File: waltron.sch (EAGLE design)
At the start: 26 parts, among them IC1 4049N, IC2 LM386, J1 On Switch, J2 9v battery, J7 8ohm speaker

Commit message: Rip up and lay out board
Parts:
- VR1: device adafruit:TRIM -> SparkFun-Retired:POTTRIM
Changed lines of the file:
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@@
 <setting verticaltext="up"/>
 </settings>
-<grid distance="0.05" unitdist="inch" unit="inch" style="lines" multiple="1" display="no" altdistance="0.01" altunitdist="inch" altunit="inch"/>
+<grid distance="0.1" unitdist="inch" unit="inch" style="lines" multiple="1" display="no" altdistance="0.01" altunitdist="inch" altunit="inch"/>
 <layers>
 <layer number="1" name="Top" color="4" fill="1" visible="no" active="no"/>
@@
 <part name="P+1" library="supply1" deviceset="V+" device=""/>
 <part name="GND1" library="supply1" deviceset="GND" device=""/>
-<part name="VR1" library="adafruit" deviceset="TRIM" device="" value="5K"/>
+<part name="VR1" library="SparkFun-Retired" deviceset="POT" device="TRIM" value="5K"/>
 <part name="J3" library="SparkFun-Connectors" deviceset="CONN_02" device=""/>
 <part name="J4" library="SparkFun-Connectors" deviceset="CONN_02" device=""/>

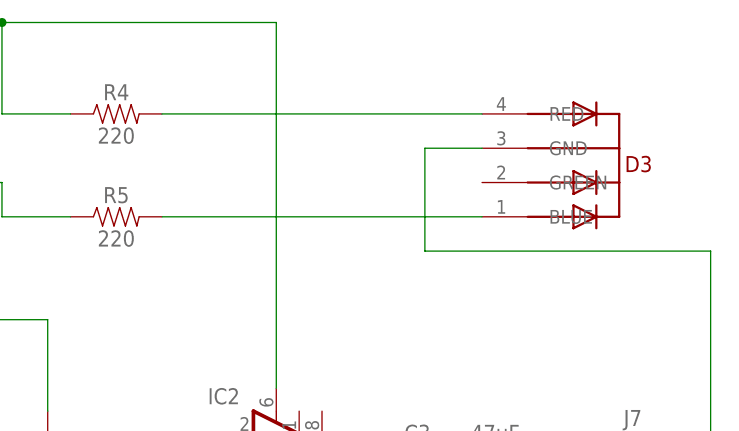
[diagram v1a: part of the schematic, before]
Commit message: Add mounting holes and swap out LED for mirrored version
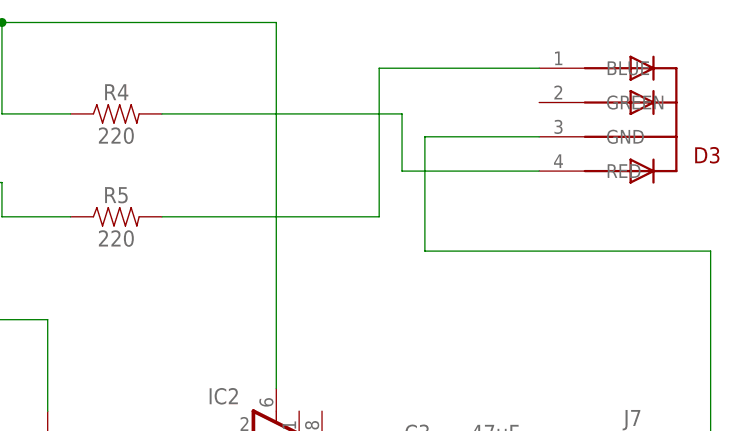
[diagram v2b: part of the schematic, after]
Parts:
- D3: device adafruit:5MMRGBLED -> tommy:5MMRGBLED
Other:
- moved on the sheet: D3
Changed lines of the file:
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@@
 <part name="J5" library="SparkFun-Connectors" deviceset="CONN_02" device=""/>
 <part name="J6" library="SparkFun-Connectors" deviceset="CONN_02" device=""/>
-<part name="D3" library="adafruit" deviceset="5MMRGBLED" device=""/>
+<part name="D3" library="tommy" deviceset="5MMRGBLED" device=""/>
 <part name="J1" library="SparkFun-Connectors" deviceset="CONN_02" device="" value="On Switch"/>
 </parts>
@@
 <attribute name="NAME" x="99.568" y="-5.08" size="1.778" layer="95" font="vector" rot="MR0"/>
 </instance>
-<instance part="D3" gate="G$1" x="208.28" y="72.39" smashed="yes" rot="MR90">
-<attribute name="NAME" x="211.973553125" y="69.741753125" size="1.778" layer="94" rot="MR0"/>
+<instance part="D3" gate="G$1" x="214.63" y="73.66" smashed="yes" rot="R270">
+<attribute name="NAME" x="219.593553125" y="72.498246875" size="1.778" layer="94" rot="R180"/>
 </instance>
 <instance part="J1" gate="G$1" x="-55.88" y="55.88" smashed="yes" rot="MR180">
@@
 <segment>
 <pinref part="R5" gate="G$1" pin="2"/>
-<wire x1="157.48" y1="64.77" x2="193.04" y2="64.77" width="0.1524" layer="91"/>
+<wire x1="157.48" y1="64.77" x2="181.61" y2="64.77" width="0.1524" layer="91"/>
+<wire x1="181.61" y1="64.77" x2="181.61" y2="81.28" width="0.1524" layer="91"/>
+<wire x1="181.61" y1="81.28" x2="199.39" y2="81.28" width="0.1524" layer="91"/>
 <pinref part="D3" gate="G$1" pin="BLUE"/>
 </segment>
@@
 <wire x1="144.78" y1="27.94" x2="144.78" y2="-48.26" width="0.1524" layer="91"/>
 <pinref part="D3" gate="G$1" pin="GND"/>
-<wire x1="193.04" y1="72.39" x2="186.69" y2="72.39" width="0.1524" layer="91"/>
-<wire x1="186.69" y1="72.39" x2="186.69" y2="60.96" width="0.1524" layer="91"/>
+<wire x1="199.39" y1="73.66" x2="186.69" y2="73.66" width="0.1524" layer="91"/>
+<wire x1="186.69" y1="73.66" x2="186.69" y2="60.96" width="0.1524" layer="91"/>
 <wire x1="186.69" y1="60.96" x2="218.44" y2="60.96" width="0.1524" layer="91"/>
 </segment>
@@
 <pinref part="R4" gate="G$1" pin="2"/>
 <pinref part="D3" gate="G$1" pin="RED"/>
-<wire x1="157.48" y1="76.2" x2="193.04" y2="76.2" width="0.1524" layer="91"/>
-</segment>
-</net>
+<wire x1="157.48" y1="76.2" x2="184.15" y2="76.2" width="0.1524" layer="91"/>
+<wire x1="184.15" y1="76.2" x2="184.15" y2="69.85" width="0.1524" layer="91"/>
+<wire x1="184.15" y1="69.85" x2="199.39" y2="69.85" width="0.1524" layer="91"/>
+</segment>
+</net>

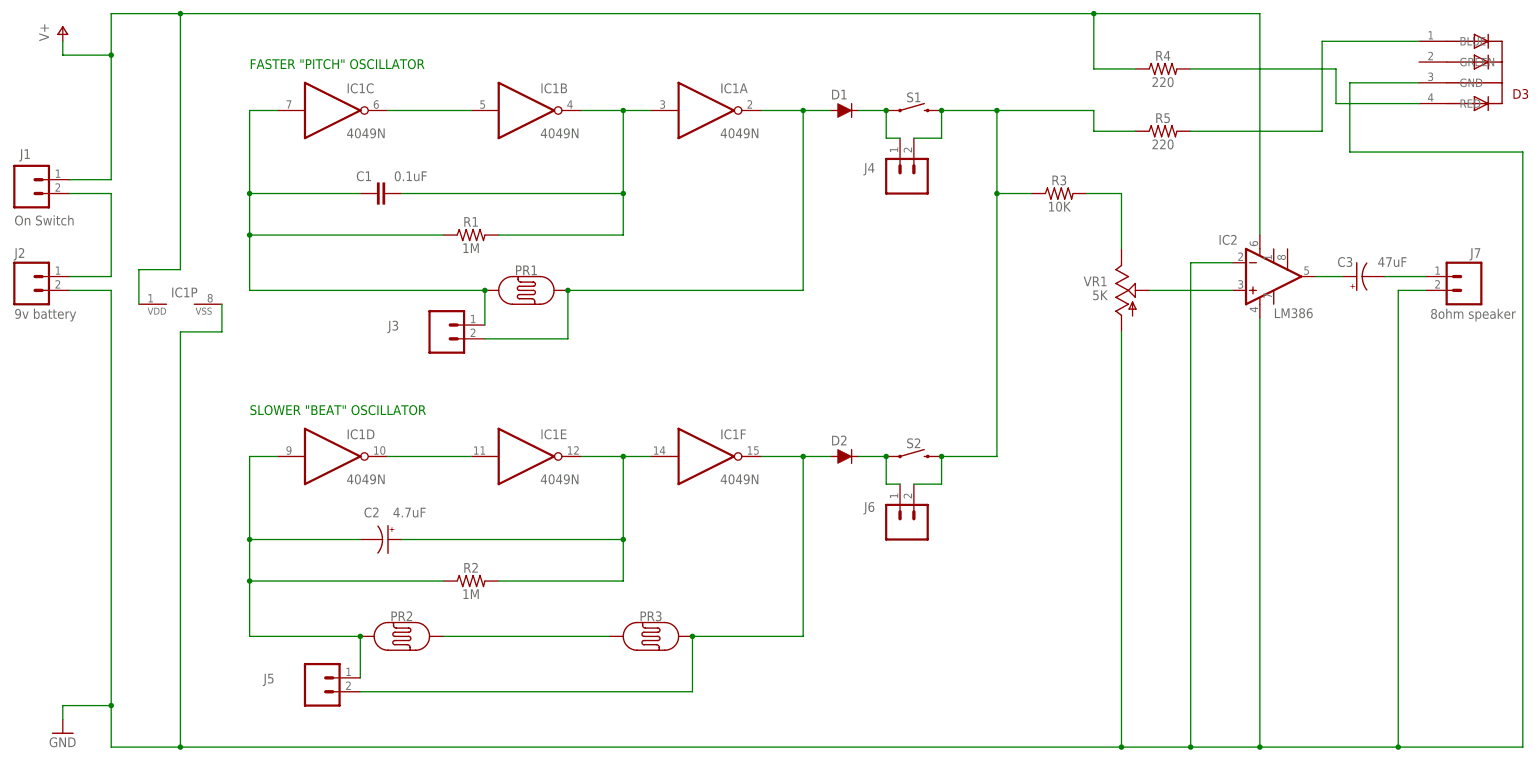
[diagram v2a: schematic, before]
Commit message: Remove headers, re-layout buttons+sensore, layout all
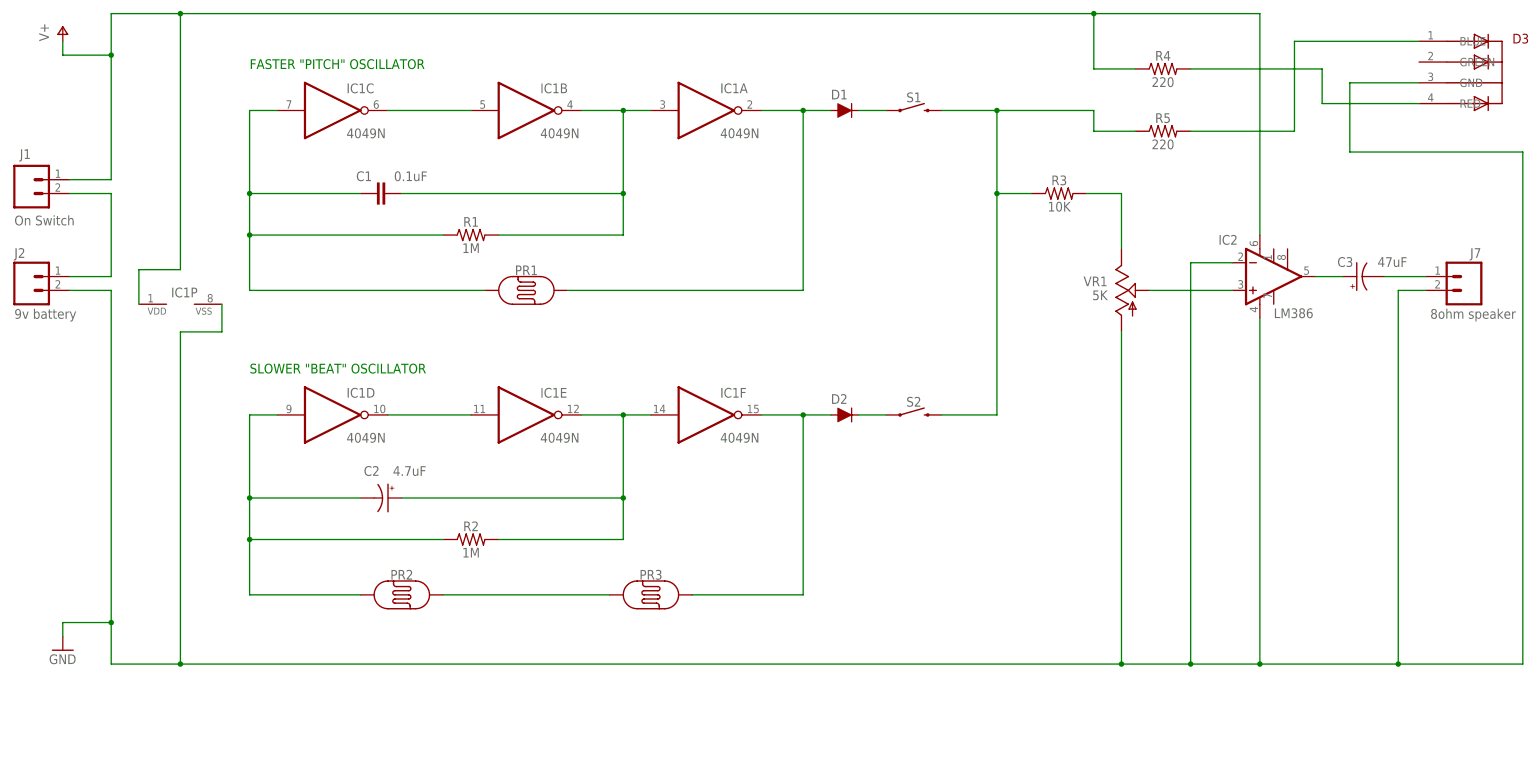
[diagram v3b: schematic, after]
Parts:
- removed J3, J4, J5, J6: (no value), SparkFun-Connectors:CONN_02
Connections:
- net N$11: no longer J6.1
- net N$12: no longer J4.2, J6.2
- net N$3: no longer J3.1
- net N$4: no longer J3.2
- net N$5: no longer J5.1
- net N$8: no longer J5.2
- net N$9: no longer J4.1
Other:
- moved on the sheet: C2, D2, IC1D, IC1E, IC1F, PR2, PR3, R2, S2

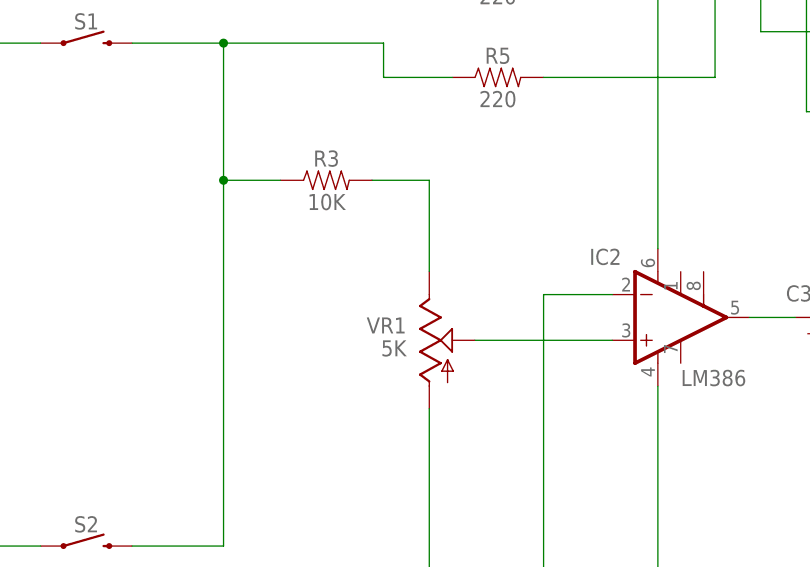
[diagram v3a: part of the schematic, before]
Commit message: Reverse volume knob rotation
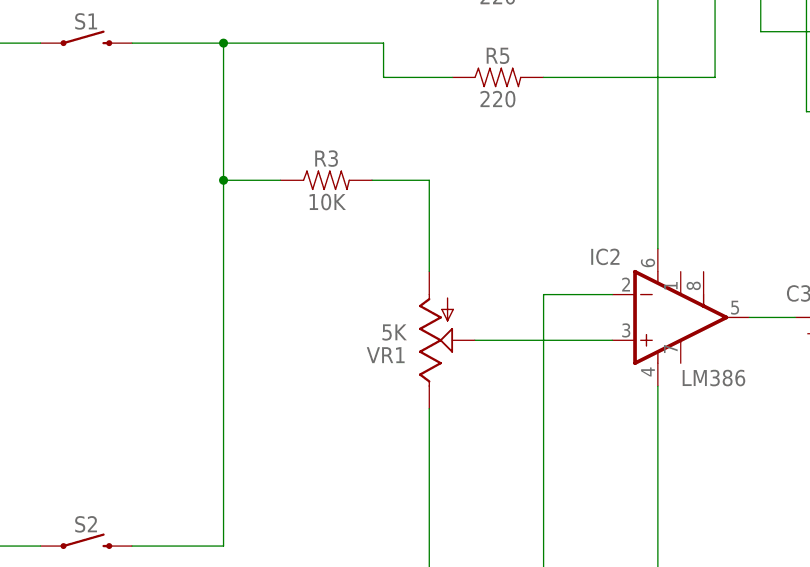
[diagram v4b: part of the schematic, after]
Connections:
- net GND: now also VR1.E; no longer VR1.A
- net N$13: now also VR1.A; no longer VR1.E
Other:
- moved on the sheet: VR1
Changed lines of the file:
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@@
 <?xml version="1.0" encoding="utf-8"?>
 <!DOCTYPE eagle SYSTEM "eagle.dtd">
-<eagle version="8.1.0">
+<eagle version="8.2.2">
 <drawing>
 <settings>
@@
 <instance part="P+1" gate="1" x="-49.53" y="83.82"/>
 <instance part="GND1" gate="1" x="-49.53" y="-30.48"/>
-<instance part="VR1" gate="G$1" x="144.78" y="35.56" smashed="yes">
-<attribute name="NAME" x="142.24" y="38.1" size="1.778" layer="95" rot="R180"/>
-<attribute name="VALUE" x="142.24" y="35.56" size="1.778" layer="96" rot="R180"/>
+<instance part="VR1" gate="G$1" x="144.78" y="35.56" smashed="yes" rot="MR180">
+<attribute name="NAME" x="142.24" y="33.02" size="1.778" layer="95" rot="MR0"/>
+<attribute name="VALUE" x="142.24" y="35.56" size="1.778" layer="96" rot="MR0"/>
 </instance>
 <instance part="D3" gate="G$1" x="214.63" y="73.66" smashed="yes" rot="R270">
@@
 <wire x1="-20.32" y1="33.02" x2="-20.32" y2="27.94" width="0.1524" layer="91"/>
 <wire x1="-20.32" y1="27.94" x2="-27.94" y2="27.94" width="0.1524" layer="91"/>
-<pinref part="VR1" gate="G$1" pin="A"/>
-<junction x="144.78" y="-33.02"/>
-<wire x1="144.78" y1="27.94" x2="144.78" y2="-33.02" width="0.1524" layer="91"/>
 <pinref part="D3" gate="G$1" pin="GND"/>
 <wire x1="199.39" y1="73.66" x2="186.69" y2="73.66" width="0.1524" layer="91"/>
 <wire x1="186.69" y1="73.66" x2="186.69" y2="60.96" width="0.1524" layer="91"/>
 <wire x1="186.69" y1="60.96" x2="218.44" y2="60.96" width="0.1524" layer="91"/>
-</segment>
-</net>
-<net name="N$13" class="0">
-<segment>
-<pinref part="R3" gate="G$1" pin="2"/>
-<wire x1="138.43" y1="53.34" x2="144.78" y2="53.34" width="0.1524" layer="91"/>
 <pinref part="VR1" gate="G$1" pin="E"/>
-<wire x1="144.78" y1="43.18" x2="144.78" y2="53.34" width="0.1524" layer="91"/>
+<wire x1="144.78" y1="27.94" x2="144.78" y2="-33.02" width="0.1524" layer="91"/>
+<junction x="144.78" y="-33.02"/>
 </segment>
 </net>
@@
 </segment>
 </net>
+<net name="N$13" class="0">
+<segment>
+<pinref part="R3" gate="G$1" pin="2"/>
+<pinref part="VR1" gate="G$1" pin="A"/>
+<wire x1="138.43" y1="53.34" x2="144.78" y2="53.34" width="0.1524" layer="91"/>
+<wire x1="144.78" y1="53.34" x2="144.78" y2="43.18" width="0.1524" layer="91"/>
+</segment>
+</net>
